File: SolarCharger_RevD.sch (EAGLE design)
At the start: 132 parts, among them CON1 CON_4X200MIL, CON2 USB_BMULTICOMP, CON3 ICSP, CON4 CON_3X100MIL, CON5 CON_3X100MIL, CON6 CON_8X200MIL, CON7 CON_2X100MIL, IC1 MCP3428, IC10 AT45DB161E, IC11 TPS54428, IC12 MCP14A0153, IC13 MCP14A0153, IC2 INA213, IC3 MIC4605-1YM, IC4 INA213, IC5 PIC18F46J50, IC6 TS6001, IC7 LMT86, IC8 24AA16, IC9 TPS62120, Q1 NX3008NBKW, Q10 NTR4101PT1G, Q11 N-FET, Q12 N-FET, Q13 N-FET, Q14 N-FET, Q15 NX3008NBKW, Q2 PSMN6R0-30YL, Q3 NX3008NBKW, Q4 NTR4101PT1G, Q5 PSMN6R0-30YL, Q6 PSMN6R0-30YL, Q7 NX3008NBKW, Q8 NX3008NBKW, Q9 NX3008NBKW, X1 ABS07-120-32.768KHZ-T, X2 ABM3-8.000MHZ-D2Y-T, X3 USB_A, X4 USB_A

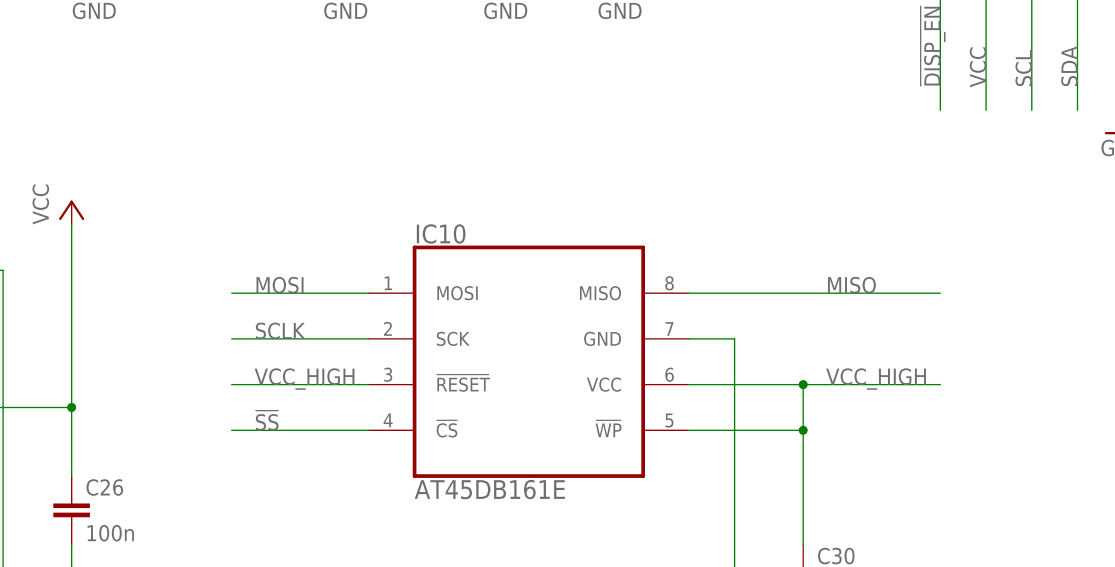
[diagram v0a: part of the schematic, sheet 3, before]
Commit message: Flash now supplied directly from VCC
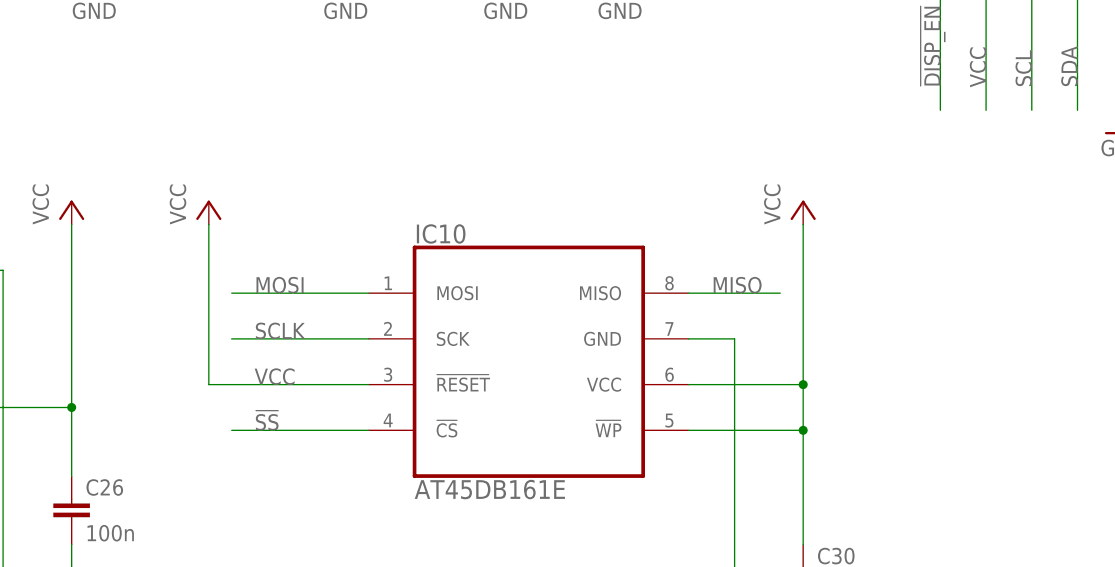
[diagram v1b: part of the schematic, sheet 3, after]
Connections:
- net VCC: now also C30.1, IC10.!RESET!, IC10.!WP!, IC10.VCC
- net VCC_HIGH: no longer C30.1, IC10.!RESET!, IC10.!WP!, IC10.VCC
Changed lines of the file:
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@@
 <part name="IC10" library="00Logic" deviceset="AT45DB161E" device=""/>
 <part name="GND84" library="00Supply" deviceset="GND" device=""/>
+<part name="P+16" library="supply1" deviceset="VCC" device=""/>
+<part name="P+17" library="supply1" deviceset="VCC" device=""/>
 </parts>
 <sheets>
@@
 <instance part="IC10" gate="G$1" x="124.46" y="63.5"/>
 <instance part="GND84" gate="1" x="147.32" y="27.94"/>
+<instance part="P+16" gate="VCC" x="154.94" y="81.28"/>
+<instance part="P+17" gate="VCC" x="88.9" y="81.28"/>
 </instances>
 <busses>
@@
 <label x="175.26" y="93.98" size="1.778" layer="95" rot="R90"/>
 </segment>
+<segment>
+<wire x1="142.24" y1="60.96" x2="154.94" y2="60.96" width="0.1524" layer="91"/>
+<pinref part="C30" gate="G$1" pin="1"/>
+<wire x1="154.94" y1="60.96" x2="154.94" y2="55.88" width="0.1524" layer="91"/>
+<wire x1="154.94" y1="55.88" x2="154.94" y2="43.18" width="0.1524" layer="91"/>
+<wire x1="142.24" y1="55.88" x2="154.94" y2="55.88" width="0.1524" layer="91"/>
+<junction x="154.94" y="55.88"/>
+<pinref part="IC10" gate="G$1" pin="VCC"/>
+<pinref part="IC10" gate="G$1" pin="!WP!"/>
+<pinref part="P+16" gate="VCC" pin="VCC"/>
+<wire x1="154.94" y1="60.96" x2="154.94" y2="78.74" width="0.1524" layer="91"/>
+<junction x="154.94" y="60.96"/>
+</segment>
+<segment>
+<wire x1="106.68" y1="60.96" x2="88.9" y2="60.96" width="0.1524" layer="91"/>
+<label x="93.98" y="60.96" size="1.778" layer="95"/>
+<pinref part="IC10" gate="G$1" pin="!RESET!"/>
+<pinref part="P+17" gate="VCC" pin="VCC"/>
+<wire x1="88.9" y1="60.96" x2="88.9" y2="78.74" width="0.1524" layer="91"/>
+</segment>
 </net>
 <net name="SCL" class="0">
@@
 <wire x1="71.12" y1="111.76" x2="55.88" y2="111.76" width="0.1524" layer="91"/>
 <label x="58.42" y="111.76" size="1.778" layer="95"/>
-</segment>
-<segment>
-<wire x1="142.24" y1="60.96" x2="154.94" y2="60.96" width="0.1524" layer="91"/>
-<wire x1="154.94" y1="60.96" x2="170.18" y2="60.96" width="0.1524" layer="91"/>
-<pinref part="C30" gate="G$1" pin="1"/>
-<wire x1="154.94" y1="60.96" x2="154.94" y2="55.88" width="0.1524" layer="91"/>
-<label x="157.48" y="60.96" size="1.778" layer="95"/>
-<junction x="154.94" y="60.96"/>
-<wire x1="154.94" y1="55.88" x2="154.94" y2="43.18" width="0.1524" layer="91"/>
-<wire x1="142.24" y1="55.88" x2="154.94" y2="55.88" width="0.1524" layer="91"/>
-<junction x="154.94" y="55.88"/>
-<pinref part="IC10" gate="G$1" pin="VCC"/>
-<pinref part="IC10" gate="G$1" pin="!WP!"/>
-</segment>
-<segment>
-<wire x1="106.68" y1="60.96" x2="91.44" y2="60.96" width="0.1524" layer="91"/>
-<label x="93.98" y="60.96" size="1.778" layer="95"/>
-<pinref part="IC10" gate="G$1" pin="!RESET!"/>
 </segment>
 </net>
@@
 <net name="MISO" class="0">
 <segment>
-<wire x1="142.24" y1="71.12" x2="170.18" y2="71.12" width="0.1524" layer="91"/>
-<label x="157.48" y="71.12" size="1.778" layer="95"/>
+<wire x1="142.24" y1="71.12" x2="152.4" y2="71.12" width="0.1524" layer="91"/>
+<label x="144.78" y="71.12" size="1.778" layer="95"/>
 <pinref part="IC10" gate="G$1" pin="MISO"/>
 </segment>
